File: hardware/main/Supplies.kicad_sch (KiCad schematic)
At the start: 10 parts, among them U601 VXO7805-1000, U602 AMS1117-3.3

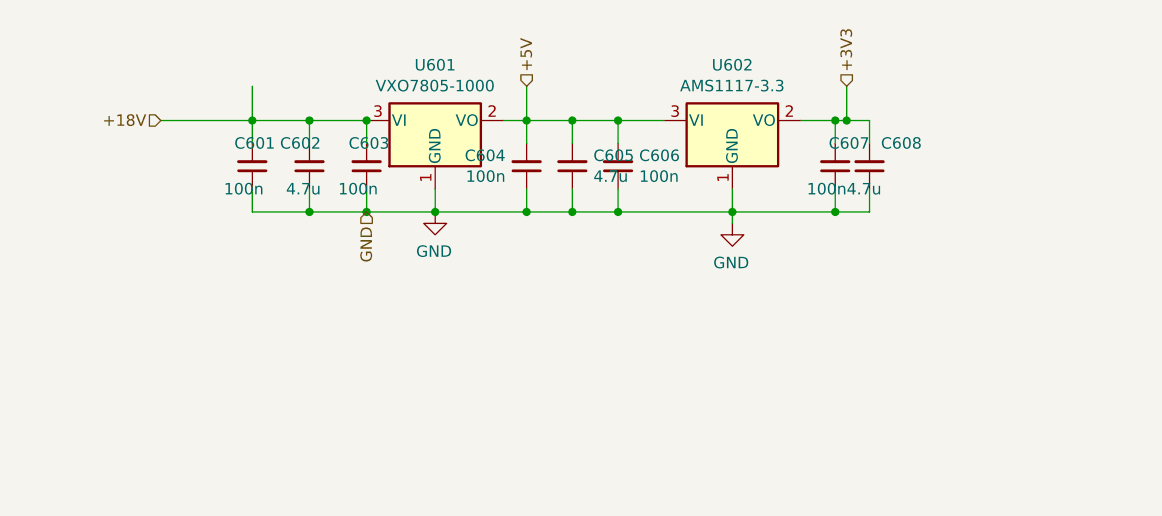
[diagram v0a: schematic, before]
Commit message: Schematics: finalize Analog Snubber and Supplies
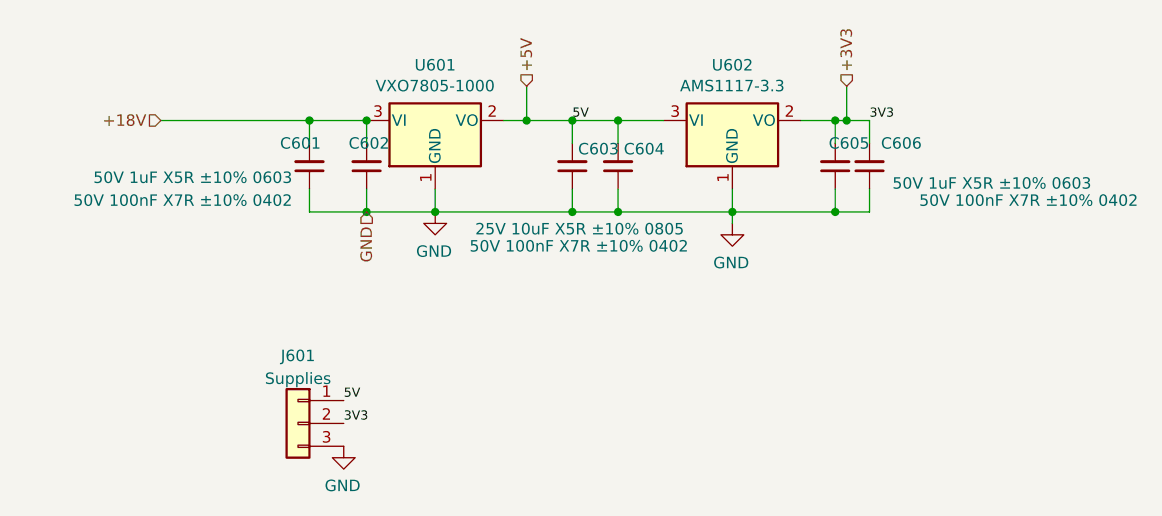
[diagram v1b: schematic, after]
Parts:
- removed C601, C604: 100n, Capacitor_SMD:C_0603_1608Metric_Pad1.08x0.95mm_HandSolder, symbol Device:C_Small
- added J601: Supplies, symbol Connector_Generic:Conn_01x03
- C601: renamed from C602; value 4.7u -> 50V 1uF X5R ±10% 0603
- C602: renamed from C603; value 100n -> 50V 100nF X7R ±10% 0402
- C603: renamed from C605; value 4.7u -> 25V 10uF X5R ±10% 0805
- C604: renamed from C606; value 100n -> 50V 100nF X7R ±10% 0402
- C605: renamed from C607; value 100n -> 50V 100nF X7R ±10% 0402
- C606: renamed from C608; value 4.7u -> 50V 1uF X5R ±10% 0603
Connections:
- net +3V3: now also J601.2 (Pin_2)
- net +5V: now also J601.1 (Pin_1)
- net GND: now also J601.3 (Pin_3)
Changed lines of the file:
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@@
   (junction (at 180.975 73.025) (diameter 0) (color 0 0 0 0)
   )
-  (junction (at 146.685 83.185) (diameter 0) (color 0 0 0 0)
-  )
   (junction (at 122.555 73.025) (diameter 0) (color 0 0 0 0)
   )
@@
   (junction (at 151.765 73.025) (diameter 0) (color 0 0 0 0)
   )
-  (junction (at 122.555 83.185) (diameter 0) (color 0 0 0 0)
-  )
   (junction (at 156.845 73.025) (diameter 0) (color 0 0 0 0)
   )
   (junction (at 180.975 83.185) (diameter 0) (color 0 0 0 0)
   )
-  (junction (at 116.205 73.025) (diameter 0) (color 0 0 0 0)
-  )
   (wire (pts (xy 169.545 83.185) (xy 156.845 83.185))
     (stroke (width 0) (type default) (color 0 0 0 0))
@@
     (stroke (width 0) (type default) (color 0 0 0 0))
   )
-  (wire (pts (xy 151.765 83.185) (xy 146.685 83.185))
+  (wire (pts (xy 136.525 83.185) (xy 151.765 83.185))
     (stroke (width 0) (type default) (color 0 0 0 0))
   )
@@
     (stroke (width 0) (type default) (color 0 0 0 0))
   )
-  (wire (pts (xy 122.555 83.185) (xy 116.205 83.185))
-    (stroke (width 0) (type default) (color 0 0 0 0))
-  )
   (wire (pts (xy 146.685 69.215) (xy 146.685 73.025))
     (stroke (width 0) (type default) (color 0 0 0 0))
@@
     (stroke (width 0) (type default) (color 0 0 0 0))
   )
-  (wire (pts (xy 116.205 75.565) (xy 116.205 73.025))
-    (stroke (width 0) (type default) (color 0 0 0 0))
-  )
-  (wire (pts (xy 146.685 83.185) (xy 136.525 83.185))
-    (stroke (width 0) (type default) (color 0 0 0 0))
-  )
-  (wire (pts (xy 122.555 73.025) (xy 116.205 73.025))
-    (stroke (width 0) (type default) (color 0 0 0 0))
-  )
   (wire (pts (xy 180.975 73.025) (xy 177.165 73.025))
     (stroke (width 0) (type default) (color 0 0 0 0))
@@
     (stroke (width 0) (type default) (color 0 0 0 0))
   )
-  (wire (pts (xy 116.205 69.215) (xy 116.205 73.025))
-    (stroke (width 0) (type default) (color 0 0 0 0))
-  )
   (wire (pts (xy 184.785 75.565) (xy 184.785 73.025))
     (stroke (width 0) (type default) (color 0 0 0 0))
@@
     (stroke (width 0) (type default) (color 0 0 0 0))
   )
-  (wire (pts (xy 146.685 75.565) (xy 146.685 73.025))
-    (stroke (width 0) (type default) (color 0 0 0 0))
-  )
   (wire (pts (xy 161.925 73.025) (xy 156.845 73.025))
     (stroke (width 0) (type default) (color 0 0 0 0))
   )
-  (wire (pts (xy 146.685 80.645) (xy 146.685 83.185))
-    (stroke (width 0) (type default) (color 0 0 0 0))
-  )
-  (wire (pts (xy 116.205 80.645) (xy 116.205 83.185))
-    (stroke (width 0) (type default) (color 0 0 0 0))
-  )
   (wire (pts (xy 128.905 80.645) (xy 128.905 83.185))
     (stroke (width 0) (type default) (color 0 0 0 0))
@@
     (stroke (width 0) (type default) (color 0 0 0 0))
   )
-  (wire (pts (xy 106.045 73.025) (xy 116.205 73.025))
+  (wire (pts (xy 106.045 73.025) (xy 122.555 73.025))
     (stroke (width 0) (type default) (color 0 0 0 0))
   )
   (wire (pts (xy 128.905 83.185) (xy 136.525 83.185))
     (stroke (width 0) (type default) (color 0 0 0 0))
+  )
+  (label "5V" (at 126.365 104.14 0)
+    (effects (font (size 1.016 1.016)) (justify left bottom))
+  )
+  (label "3V3" (at 184.785 73.025 0)
+    (effects (font (size 1.016 1.016)) (justify left bottom))
+  )
+  (label "3V3" (at 126.365 106.68 0)
+    (effects (font (size 1.016 1.016)) (justify left bottom))
+  )
+  (label "5V" (at 151.765 73.025 0)
+    (effects (font (size 1.016 1.016)) (justify left bottom))
   )
   (hierarchical_label "GND" (shape input) (at 128.905 83.185 270)
@@
     (pin "3")
   )
+  (symbol (lib_id "power:GND") (at 126.365 109.22 0) (mirror y) (unit 1)
+    (in_bom yes) (on_board yes)
+    (property "Reference" "#PWR0601" (id 0) (at 126.365 115.57 0)
+      (effects (font (size 1.27 1.27)) hide)
+    )
+    (property "Value" "GND" (id 1) (at 126.238 113.6142 0))
+    (property "Footprint" "" (id 2) (at 126.365 109.22 0)
+      (effects (font (size 1.27 1.27)) hide)
+    )
+    (property "Datasheet" "" (id 3) (at 126.365 109.22 0)
+      (effects (font (size 1.27 1.27)) hide)
+    )
+    (pin "1")
+  )
   (symbol (lib_id "Device:C_Small") (at 180.975 78.105 0) (mirror x) (unit 1)
     (in_bom yes) (on_board yes)
-    (property "Reference" "C607" (id 0) (at 184.785 75.565 0)
-      (effects (font (size 1.27 1.27)) (justify right))
-    )
-    (property "Value" "100n" (id 1) (at 182.245 80.645 0)
+    (property "Reference" "C605" (id 0) (at 184.785 75.565 0)
+      (effects (font (size 1.27 1.27)) (justify right))
+    )
+    (property "Value" "50V 100nF X7R ±10% 0402" (id 1) (at 214.63 81.915 0)
       (effects (font (size 1.27 1.27)) (justify right))
     )
@@
   (symbol (lib_id "power:GND") (at 136.525 83.185 0) (mirror y) (unit 1)
     (in_bom yes) (on_board yes)
-    (property "Reference" "#PWR0179" (id 0) (at 136.525 89.535 0)
+    (property "Reference" "#PWR0602" (id 0) (at 136.525 89.535 0)
       (effects (font (size 1.27 1.27)) hide)
     )
@@
     (pin "1")
   )
-  (symbol (lib_id "Device:C_Small") (at 146.685 78.105 0) (mirror x) (unit 1)
-    (in_bom yes) (on_board yes)
-    (property "Reference" "C604" (id 0) (at 144.3482 76.9366 0)
-      (effects (font (size 1.27 1.27)) (justify right))
-    )
-    (property "Value" "100n" (id 1) (at 144.3482 79.248 0)
-      (effects (font (size 1.27 1.27)) (justify right))
-    )
-    (property "Footprint" "Capacitor_SMD:C_0603_1608Metric_Pad1.08x0.95mm_HandSolder" (id 2) (at 146.685 78.105 0)
-      (effects (font (size 1.27 1.27)) hide)
-    )
-    (property "Datasheet" "~" (id 3) (at 146.685 78.105 0)
-      (effects (font (size 1.27 1.27)) hide)
-    )
-    (pin "1")
-    (pin "2")
+  (symbol (lib_id "Connector_Generic:Conn_01x03") (at 121.285 106.68 0) (mirror y) (unit 1)
+    (in_bom yes) (on_board yes) (fields_autoplaced)
+    (property "Reference" "J601" (id 0) (at 121.285 99.1702 0))
+    (property "Value" "Supplies" (id 1) (at 121.285 101.7071 0))
+    (property "Footprint" "" (id 2) (at 121.285 106.68 0)
+      (effects (font (size 1.27 1.27)) hide)
+    )
+    (property "Datasheet" "~" (id 3) (at 121.285 106.68 0)
+      (effects (font (size 1.27 1.27)) hide)
+    )
+    (pin "1")
+    (pin "2")
+    (pin "3")
   )
   (symbol (lib_id "Device:C_Small") (at 128.905 78.105 0) (mirror x) (unit 1)
     (in_bom yes) (on_board yes)
-    (property "Reference" "C603" (id 0) (at 131.445 75.565 0)
-      (effects (font (size 1.27 1.27)) (justify right))
-    )
-    (property "Value" "100n" (id 1) (at 130.175 80.645 0)
+    (property "Reference" "C602" (id 0) (at 131.445 75.565 0)
+      (effects (font (size 1.27 1.27)) (justify right))
+    )
+    (property "Value" "50V 100nF X7R ±10% 0402" (id 1) (at 120.65 81.915 0)
       (effects (font (size 1.27 1.27)) (justify right))
     )
@@
   (symbol (lib_id "Device:C_Small") (at 156.845 78.105 180) (unit 1)
     (in_bom yes) (on_board yes)
-    (property "Reference" "C606" (id 0) (at 159.1818 76.9366 0)
-      (effects (font (size 1.27 1.27)) (justify right))
-    )
-    (property "Value" "100n" (id 1) (at 159.1818 79.248 0)
+    (property "Reference" "C604" (id 0) (at 157.48 76.2 0)
+      (effects (font (size 1.27 1.27)) (justify right))
+    )
+    (property "Value" "50V 100nF X7R ±10% 0402" (id 1) (at 140.335 86.995 0)
       (effects (font (size 1.27 1.27)) (justify right))
     )
@@
     (pin "2")
   )
-  (symbol (lib_id "Device:C_Small") (at 116.205 78.105 0) (mirror x) (unit 1)
-    (in_bom yes) (on_board yes)
-    (property "Reference" "C601" (id 0) (at 118.745 75.565 0)
-      (effects (font (size 1.27 1.27)) (justify right))
-    )
-    (property "Value" "100n" (id 1) (at 117.475 80.645 0)
-      (effects (font (size 1.27 1.27)) (justify right))
-    )
-    (property "Footprint" "Capacitor_SMD:C_0603_1608Metric_Pad1.08x0.95mm_HandSolder" (id 2) (at 116.205 78.105 0)
-      (effects (font (size 1.27 1.27)) hide)
-    )
-    (property "Datasheet" "~" (id 3) (at 116.205 78.105 0)
-      (effects (font (size 1.27 1.27)) hide)
-    )
-    (pin "1")
-    (pin "2")
-  )
   (symbol (lib_id "Device:C_Small") (at 122.555 78.105 0) (mirror x) (unit 1)
     (in_bom yes) (on_board yes)
-    (property "Reference" "C602" (id 0) (at 123.825 75.565 0)
-      (effects (font (size 1.27 1.27)) (justify right))
-    )
-    (property "Value" "4.7u" (id 1) (at 123.825 80.645 0)
+    (property "Reference" "C601" (id 0) (at 123.825 75.565 0)
+      (effects (font (size 1.27 1.27)) (justify right))
+    )
+    (property "Value" "50V 1uF X5R ±10% 0603" (id 1) (at 120.65 79.375 0)
       (effects (font (size 1.27 1.27)) (justify right))
     )
@@
   (symbol (lib_id "Device:C_Small") (at 184.785 78.105 180) (unit 1)
     (in_bom yes) (on_board yes)
-    (property "Reference" "C608" (id 0) (at 186.055 75.565 0)
-      (effects (font (size 1.27 1.27)) (justify right))
-    )
-    (property "Value" "4.7u" (id 1) (at 182.245 80.645 0)
+    (property "Reference" "C606" (id 0) (at 186.055 75.565 0)
+      (effects (font (size 1.27 1.27)) (justify right))
+    )
+    (property "Value" "50V 1uF X5R ±10% 0603" (id 1) (at 187.325 80.01 0)
       (effects (font (size 1.27 1.27)) (justify right))
     )
@@
   (symbol (lib_id "Device:C_Small") (at 151.765 78.105 180) (unit 1)
     (in_bom yes) (on_board yes)
-    (property "Reference" "C605" (id 0) (at 154.1018 76.9366 0)
-      (effects (font (size 1.27 1.27)) (justify right))
-    )
-    (property "Value" "4.7u" (id 1) (at 154.1018 79.248 0)
+    (property "Reference" "C603" (id 0) (at 152.4 76.2 0)
+      (effects (font (size 1.27 1.27)) (justify right))
+    )
+    (property "Value" "25V 10uF X5R ±10% 0805" (id 1) (at 140.97 85.09 0)
       (effects (font (size 1.27 1.27)) (justify right))
     )
@@
   (symbol (lib_id "power:GND") (at 169.545 84.455 0) (mirror y) (unit 1)
     (in_bom yes) (on_board yes)
-    (property "Reference" "#PWR0180" (id 0) (at 169.545 90.805 0)
-      (effects (font (size 1.27 1.27)) hide)
-    )
+    (property "Reference" "#PWR0603" (id 0) (at 169.545 90.805 0)
+      (effects (font (size 1.27 1.27)) hide)
+    )

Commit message: Schematics: Run DRC and fix errors and some warnings, also added Zenite kicad library repo as submodule
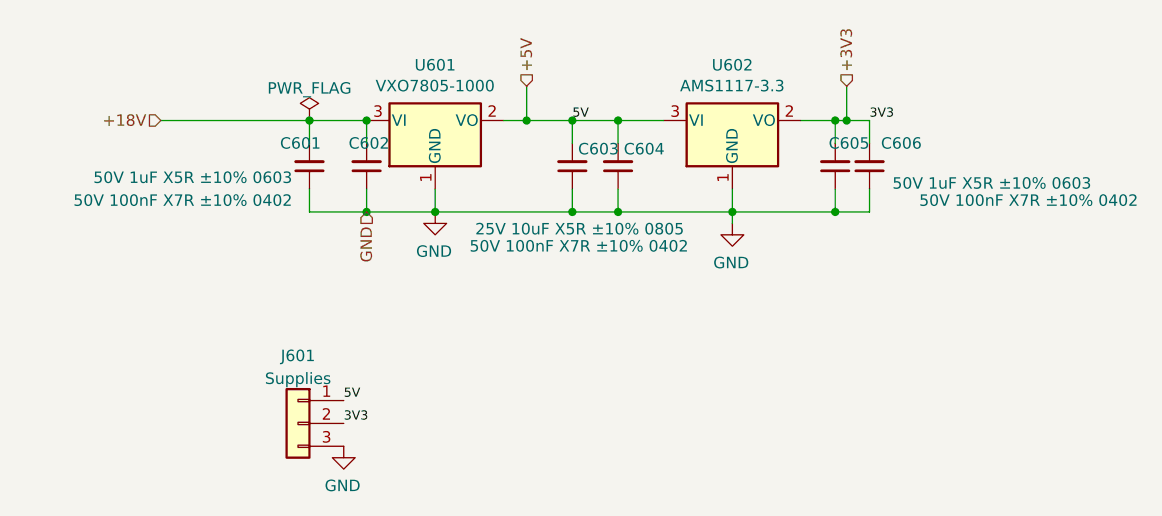
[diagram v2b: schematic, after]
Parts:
- J601: footprint (none) -> Connector_PinHeader_2.54mm:PinHeader_1x03_P2.54mm_Vertical
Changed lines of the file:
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@@
     (pin "2")
+  )
+  (symbol (lib_id "power:PWR_FLAG") (at 122.555 73.025 0) (unit 1)
+    (in_bom yes) (on_board yes) (fields_autoplaced)
+    (property "Reference" "#FLG0601" (id 0) (at 122.555 71.12 0)
+      (effects (font (size 1.27 1.27)) hide)
+    )
+    (property "Value" "PWR_FLAG" (id 1) (at 122.555 69.4492 0))
+    (property "Footprint" "" (id 2) (at 122.555 73.025 0)
+      (effects (font (size 1.27 1.27)) hide)
+    )
+    (property "Datasheet" "~" (id 3) (at 122.555 73.025 0)
+      (effects (font (size 1.27 1.27)) hide)
+    )
+    (pin "1")
   )
   (symbol (lib_id "power:GND") (at 136.525 83.185 0) (mirror y) (unit 1)
@@
     (property "Reference" "J601" (id 0) (at 121.285 99.1702 0))
     (property "Value" "Supplies" (id 1) (at 121.285 101.7071 0))
-    (property "Footprint" "" (id 2) (at 121.285 106.68 0)
+    (property "Footprint" "Connector_PinHeader_2.54mm:PinHeader_1x03_P2.54mm_Vertical" (id 2) (at 121.285 106.68 0)
       (effects (font (size 1.27 1.27)) hide)
     )

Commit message: Layout: Organizing components
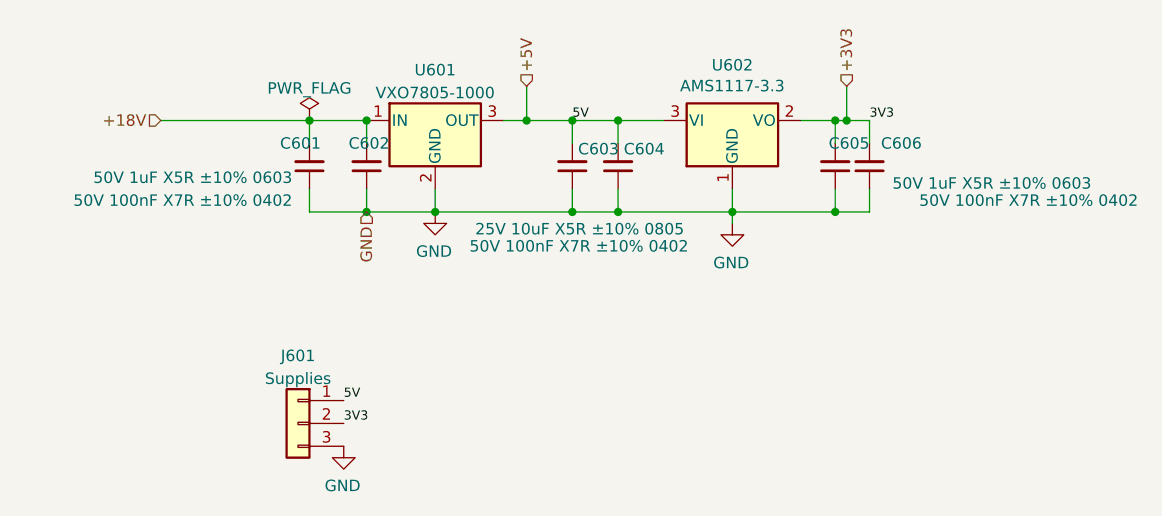
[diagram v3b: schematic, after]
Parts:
- removed U601: VXO7805-1000, Zenite:TO-220-3_Horizontal_TabDown_SMD, symbol Regulator_Linear:AP1117-15
- added U601: VXO7805-1000, Zenite:TO-220-3_Horizontal_TabDown_SMD, symbol Regulator_Linear:L7805
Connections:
- net +18V: now also U601.1 (IN)
- net +5V: now also U601.3 (OUT)
- net GND: now also U601.2 (GND)
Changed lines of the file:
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@@
   (junction (at 169.545 83.185) (diameter 0) (color 0 0 0 0)
   )
+  (junction (at 151.765 73.025) (diameter 0) (color 0 0 0 0)
+  )
+  (junction (at 156.845 73.025) (diameter 0) (color 0 0 0 0)
+  )
+  (junction (at 180.975 83.185) (diameter 0) (color 0 0 0 0)
+  )
   (junction (at 128.905 73.025) (diameter 0) (color 0 0 0 0)
-  )
-  (junction (at 151.765 73.025) (diameter 0) (color 0 0 0 0)
-  )
-  (junction (at 156.845 73.025) (diameter 0) (color 0 0 0 0)
-  )
-  (junction (at 180.975 83.185) (diameter 0) (color 0 0 0 0)
   )
   (wire (pts (xy 169.545 83.185) (xy 156.845 83.185))
@@
     )
     (pin "1")
+  )
+  (symbol (lib_id "Regulator_Linear:L7805") (at 136.525 73.025 0) (unit 1)
+    (in_bom yes) (on_board yes) (fields_autoplaced)
+    (property "Reference" "U601" (id 0) (at 136.525 67.4202 0))
+    (property "Value" "VXO7805-1000" (id 1) (at 136.525 69.9571 0))
+    (property "Footprint" "Zenite:TO-220-3_Horizontal_TabDown_SMD" (id 2) (at 137.16 76.835 0)
+      (effects (font (size 1.27 1.27) italic) (justify left) hide)
+    )
+    (property "Datasheet" "https://www.mouser.com/ProductDetail/CUI-Inc/VXO7805-1000?qs=HXFqYaX1Q2zTUq5iRuYtuQ%3D%3D" (id 3) (at 136.525 74.295 0)
+      (effects (font (size 1.27 1.27)) hide)
+    )
+    (pin "1")
+    (pin "2")
+    (pin "3")
   )
   (symbol (lib_id "power:GND") (at 136.525 83.185 0) (mirror y) (unit 1)
@@
     (pin "2")
   )
-  (symbol (lib_id "Regulator_Linear:AP1117-15") (at 136.525 73.025 0) (unit 1)
-    (in_bom yes) (on_board yes)
-    (property "Reference" "U601" (id 0) (at 136.525 66.8782 0))
-    (property "Value" "VXO7805-1000" (id 1) (at 136.525 69.1896 0))
-    (property "Footprint" "Zenite:TO-220-3_Horizontal_TabDown_SMD" (id 2) (at 136.525 67.945 0)
-      (effects (font (size 1.27 1.27)) hide)
-    )
-    (property "Datasheet" "https://www.mouser.com/ProductDetail/CUI-Inc/VXO7805-1000?qs=HXFqYaX1Q2zTUq5iRuYtuQ%3D%3D" (id 3) (at 139.065 79.375 0)
-      (effects (font (size 1.27 1.27)) hide)
-    )
-    (pin "1")
-    (pin "2")
-    (pin "3")
-  )
   (symbol (lib_id "power:GND") (at 169.545 84.455 0) (mirror y) (unit 1)
